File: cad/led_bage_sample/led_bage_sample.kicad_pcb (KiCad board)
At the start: 4 copper layers, 28.4 x 22.1 mm, 136 parts, among them J1 Conn_01x06, Q2 AO4407A, U1 74AHCT1G125, U2 74AHCT1G125

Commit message: sync
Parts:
- moved C19 12.6 mm to (64.6, 52.0), turned to 45 degrees
- moved C23 12.6 mm to (52.1, 65.0), turned to 45 degrees
- moved C7 3.42 mm to (55.2, 52.0), turned to 45 degrees
- moved C1 3.40 mm to (58.4, 52.0), turned to 45 degrees
- moved C20 3.37 mm to (61.5, 52.0), turned to 45 degrees
- moved C13 3.35 mm to (52.1, 52.0), turned to 45 degrees
- moved C25 3.35 mm to (55.2, 65.0), turned to 45 degrees
- moved C24 3.34 mm to (58.4, 65.0), turned to 45 degrees
- moved C12 3.29 mm to (64.6, 65.0), turned to 45 degrees
- moved C18 3.27 mm to (61.5, 65.0), turned to 45 degrees
- moved C2 1.24 mm to (58.4, 55.2), turned to 45 degrees
- moved C8 1.24 mm to (55.2, 55.2), turned to 45 degrees
- moved C15 1.24 mm to (61.5, 55.2), turned to 45 degrees
- moved C14 1.24 mm to (52.1, 55.2), turned to 45 degrees
- moved C3 1.24 mm to (64.6, 55.2), turned to 45 degrees
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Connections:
- C25 pad 1: GND -> VDD_S
- C25 pad 2: VDD_S -> GND
- U1 pad 5: VDD_S -> DATA1
- U2 pad 5: VDD_S -> DATA1
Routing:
- net GND: track 116.7 -> 18.8 mm, vias 40 -> 104
- net VDD_S: track 71.4 -> 5.73 mm, vias 30 -> 104
- net Net-(D1-DIN): track 22.5 -> 0.00 mm, vias 1 -> 0
- net Net-(D51-DIN): track 8.98 -> 0.00 mm, vias 1 -> 0
- net VDD: track 13.2 -> 9.75 mm
- net Net-(D90-DOUT): track 0.78 -> 3.63 mm
- net Net-(D70-DOUT): track 0.77 -> 3.58 mm
- net Net-(D30-DOUT): track 0.77 -> 3.58 mm
- net Net-(D10-DOUT): track 0.77 -> 3.58 mm
- net Net-(D68-DOUT): track 0.71 -> 2.81 mm
- net Net-(D28-DOUT): track 0.71 -> 2.81 mm
- net Net-(D8-DOUT): track 0.71 -> 2.81 mm
- net Net-(D48-DOUT): track 0.71 -> 2.81 mm
- net Net-(D66-DOUT): track 0.71 -> 2.81 mm
- net Net-(D43-DOUT): track 0.71 -> 2.81 mm
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
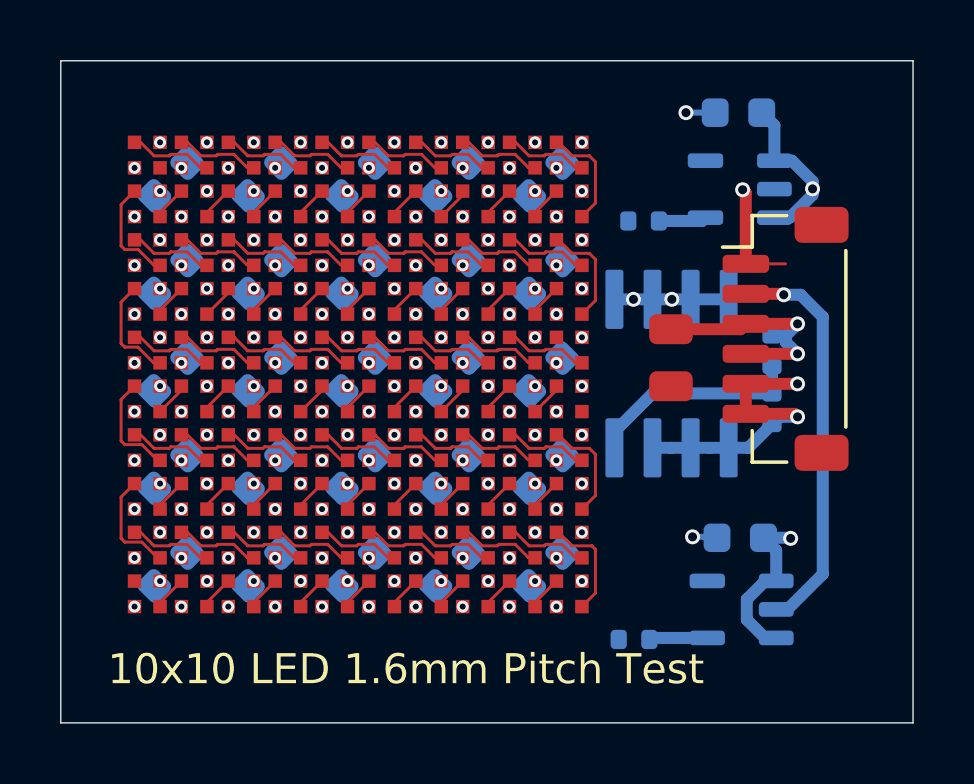
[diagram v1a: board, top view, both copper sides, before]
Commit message: feat: scale protection circuit toward 2500-LED main board
Add Si7145DP P-FET (U1) and SnapEDA-imported library table (fp-lib-table)
to the main board. WIP: U1 pin-to-net mapping is incorrect — drain pads
currently land on VDD instead of VDD_S, so the FET is shorted across
itself and not actually protecting anything yet.

Add three pcbnew automation scripts to support the build:
- stitch_power_planes.py: checkerboard via stitching across In1.Cu/In2.Cu
- add_thermal_vias.py: drops thermal via grid under exposed pads
- place_bulk_caps.py: clones a template cap across the LED bbox

Sample board updated alongside the main board for prototyping continuity.
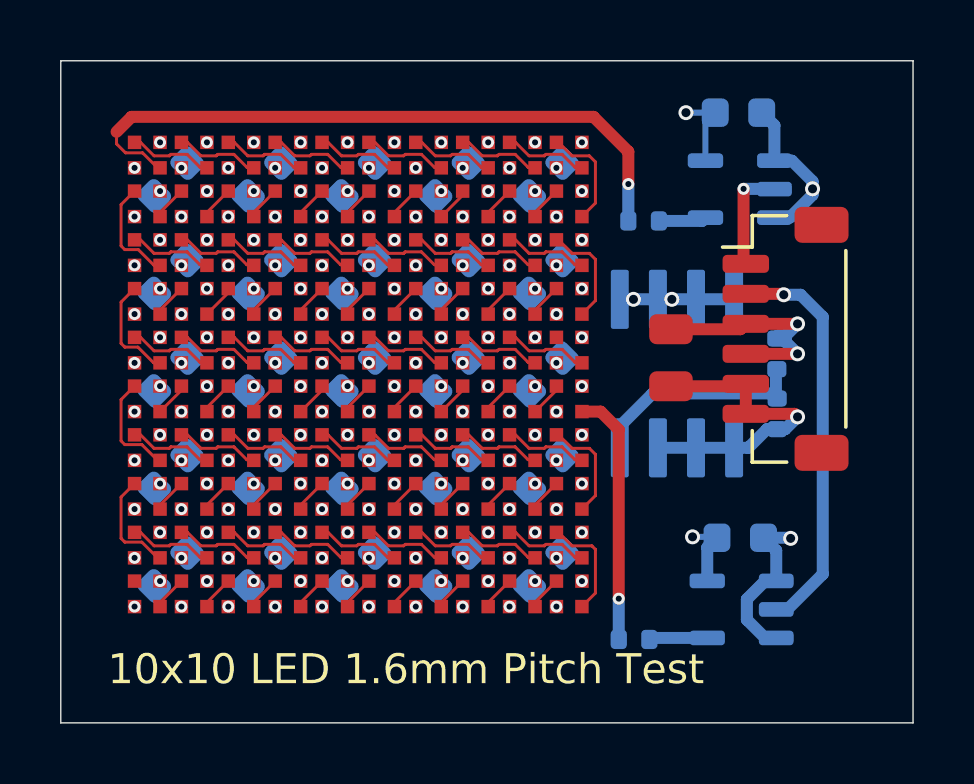
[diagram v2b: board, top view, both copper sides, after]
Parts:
- moved R3 0.24 mm to (72.3, 59.8)
- moved R4 0.19 mm to (72.3, 57.8)
- moved Q2 0.18 mm to (69.0, 58.5)
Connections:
- U1 pad 5: DATA1 -> VDD_S
- U2 pad 5: DATA1 -> VDD_S
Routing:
- net Net-(D1-DIN): track 0.00 -> 22.0 mm, vias 0 -> 1
- net Net-(D51-DIN): track 0.00 -> 8.47 mm, vias 0 -> 1
- net VDD_S: track 5.73 -> 8.70 mm
- net GND: track 18.8 -> 17.9 mm
- net Net-(Q2-Pad4): track 7.23 -> 6.44 mm
- net VDD: track 9.75 -> 10.3 mm, vias 2 -> 1
